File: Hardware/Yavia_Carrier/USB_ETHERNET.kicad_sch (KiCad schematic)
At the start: 51 parts, among them J8 USB, J9 Ethernet, T1 HX1188NL, U7 LAN9512i, Y1 25MHZ

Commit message: add ldd circuit
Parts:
- renumbered C14 to C19, C15 to C20, C16 to C21, C17 to C22, C18 to C23, C19 to C24, C20 to C25, C21 to C26, C22 to C27, C23 to C28, C24 to C29, C25 to C30, C26 to C31, C27 to C32, C28 to C33, C29 to C34, C30 to C35, C31 to C36, C32 to C37, C33 to C38, C34 to C39, C35 to C40, L3 to L5, L4 to L6, U7 to U8
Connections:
- net +3V3: now also L5.1

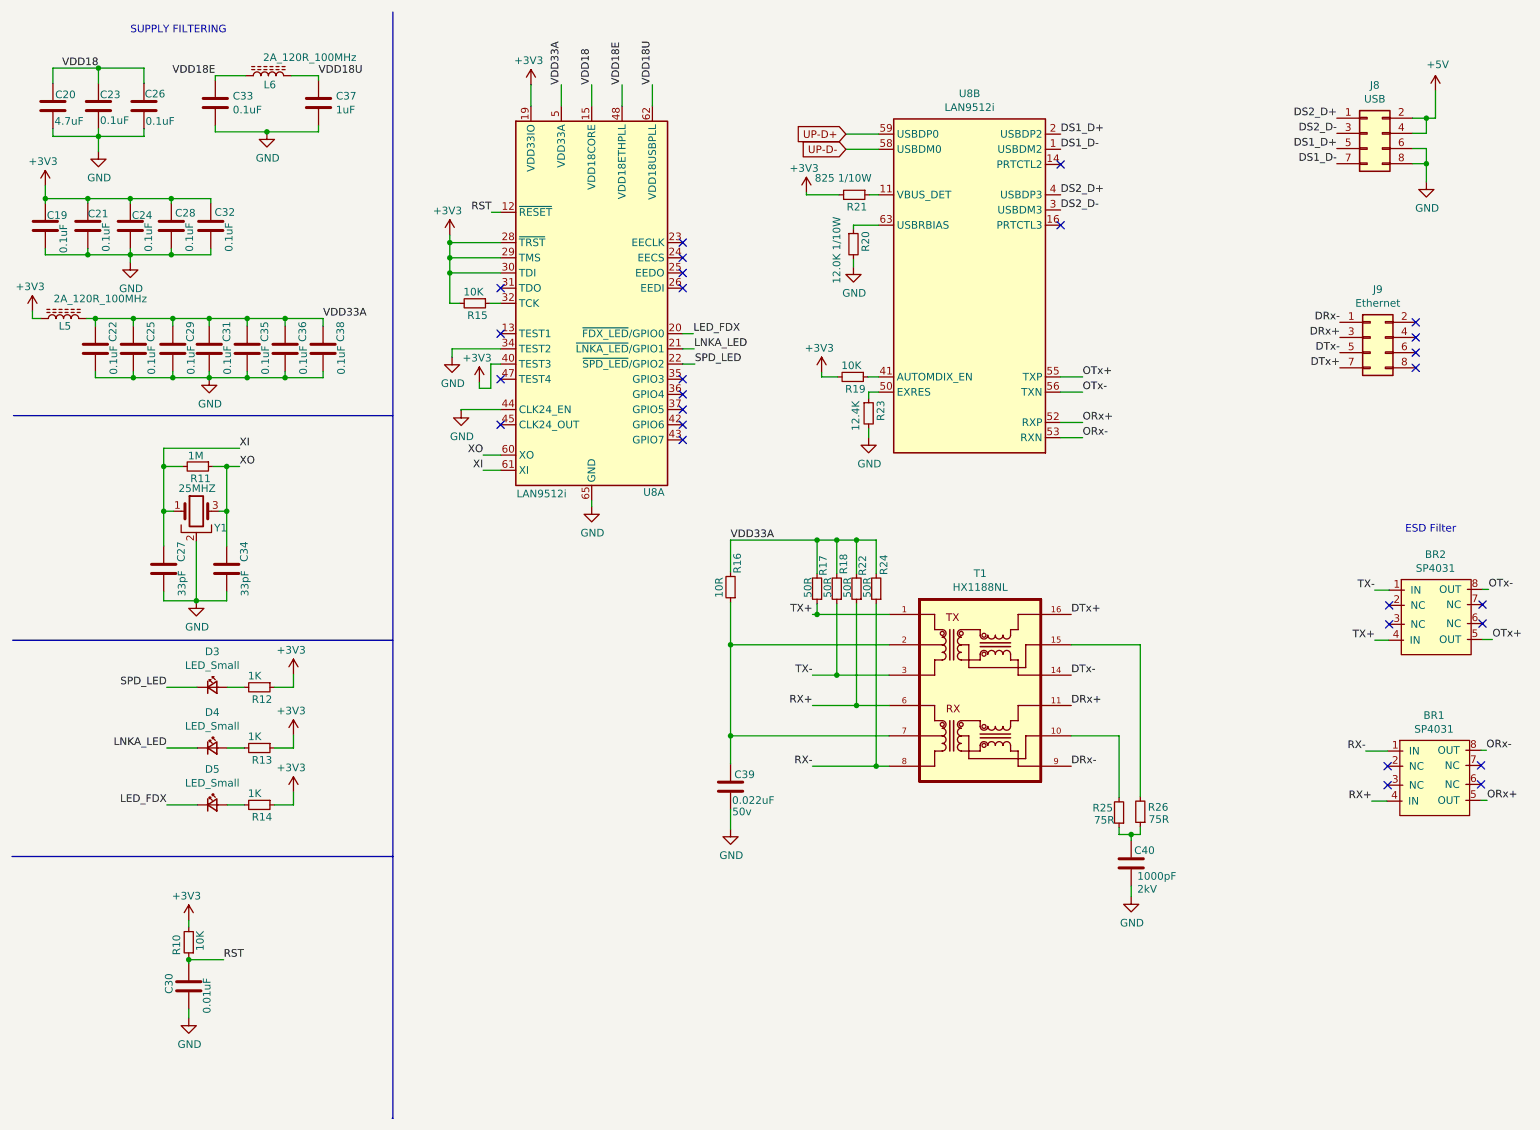
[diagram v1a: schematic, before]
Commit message: Fix U1 symbol & started pcb
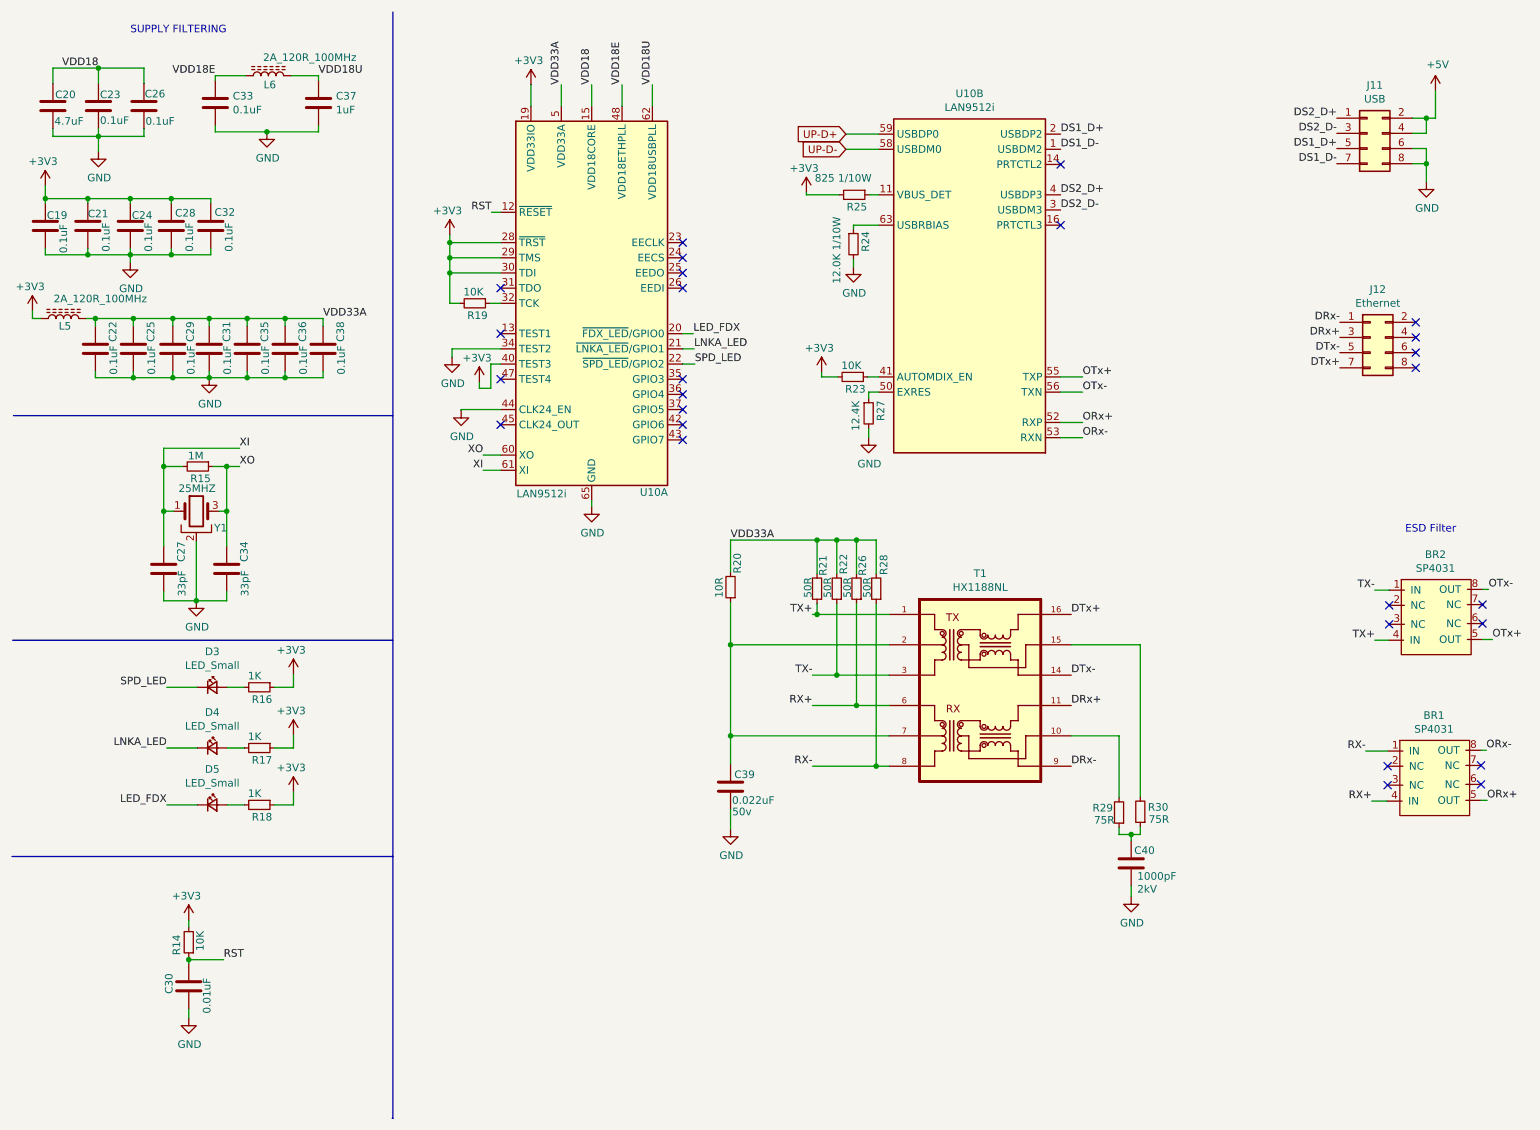
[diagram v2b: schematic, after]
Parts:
- C19, C20, C21, C22, C23, C24, C25, C26, C27, C28, C29, C30, C31, C32, C33, C34, C35, C36, C37, C38: footprint Capacitor_SMD:C_0603_1608Metric_Pad1.05x0.95mm_HandSolder -> Capacitor_SMD:C_0603_1608Metric_Pad1.08x0.95mm_HandSolder
- J11: renamed from J8; footprint RPi-Carrier:DF11-8DP-2DSA(08) -> Yavia_carrier:DF11-8DP-2DSA(08)
- J12: renamed from J9; footprint RPi-Carrier:DF11-8DP-2DSA(08) -> Yavia_carrier:DF11-8DP-2DSA(08)
- R14: renamed from R10; footprint Resistor_SMD:R_0603_1608Metric_Pad1.05x0.95mm_HandSolder -> Resistor_SMD:R_0603_1608Metric_Pad0.98x0.95mm_HandSolder
- R15: renamed from R11; footprint Resistor_SMD:R_0603_1608Metric_Pad1.05x0.95mm_HandSolder -> Resistor_SMD:R_0603_1608Metric_Pad0.98x0.95mm_HandSolder
- R16: renamed from R12; footprint Resistor_SMD:R_0603_1608Metric_Pad1.05x0.95mm_HandSolder -> Resistor_SMD:R_0603_1608Metric_Pad0.98x0.95mm_HandSolder
- R17: renamed from R13; footprint Resistor_SMD:R_0603_1608Metric_Pad1.05x0.95mm_HandSolder -> Resistor_SMD:R_0603_1608Metric_Pad0.98x0.95mm_HandSolder
- R18: renamed from R14; footprint Resistor_SMD:R_0603_1608Metric_Pad1.05x0.95mm_HandSolder -> Resistor_SMD:R_0603_1608Metric_Pad0.98x0.95mm_HandSolder
- R19: renamed from R15; footprint Resistor_SMD:R_0603_1608Metric_Pad1.05x0.95mm_HandSolder -> Resistor_SMD:R_0603_1608Metric_Pad0.98x0.95mm_HandSolder
- R20: renamed from R16; footprint Resistor_SMD:R_0603_1608Metric_Pad1.05x0.95mm_HandSolder -> Resistor_SMD:R_0603_1608Metric_Pad0.98x0.95mm_HandSolder
- R21: renamed from R17; footprint Resistor_SMD:R_0603_1608Metric_Pad1.05x0.95mm_HandSolder -> Resistor_SMD:R_0603_1608Metric_Pad0.98x0.95mm_HandSolder
- R22: renamed from R18; footprint Resistor_SMD:R_0603_1608Metric_Pad1.05x0.95mm_HandSolder -> Resistor_SMD:R_0603_1608Metric_Pad0.98x0.95mm_HandSolder
- R23: renamed from R19; footprint Resistor_SMD:R_0603_1608Metric_Pad1.05x0.95mm_HandSolder -> Resistor_SMD:R_0603_1608Metric_Pad0.98x0.95mm_HandSolder
- R24: renamed from R20; footprint Resistor_SMD:R_0603_1608Metric_Pad1.05x0.95mm_HandSolder -> Resistor_SMD:R_0603_1608Metric_Pad0.98x0.95mm_HandSolder
- R25: renamed from R21; footprint Resistor_SMD:R_0603_1608Metric_Pad1.05x0.95mm_HandSolder -> Resistor_SMD:R_0603_1608Metric_Pad0.98x0.95mm_HandSolder
- R26: renamed from R22; footprint Resistor_SMD:R_0603_1608Metric_Pad1.05x0.95mm_HandSolder -> Resistor_SMD:R_0603_1608Metric_Pad0.98x0.95mm_HandSolder
- R27: renamed from R23; footprint Resistor_SMD:R_0603_1608Metric_Pad1.05x0.95mm_HandSolder -> Resistor_SMD:R_0603_1608Metric_Pad0.98x0.95mm_HandSolder
- R28: renamed from R24; footprint Resistor_SMD:R_0603_1608Metric_Pad1.05x0.95mm_HandSolder -> Resistor_SMD:R_0603_1608Metric_Pad0.98x0.95mm_HandSolder
- R29: renamed from R25; footprint Resistor_SMD:R_0603_1608Metric_Pad1.05x0.95mm_HandSolder -> Resistor_SMD:R_0603_1608Metric_Pad0.98x0.95mm_HandSolder
- R30: renamed from R26; footprint Resistor_SMD:R_0603_1608Metric_Pad1.05x0.95mm_HandSolder -> Resistor_SMD:R_0603_1608Metric_Pad0.98x0.95mm_HandSolder
- T1: footprint RPi-Carrier:HXXXX -> Yavia_carrier:HXXXX
- renumbered U8 to U10
